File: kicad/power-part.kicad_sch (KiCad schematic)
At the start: 52 parts, among them Q10 BSS84, Q11 BSS123N, Q12 ZXMP10A17GTA, Q2 IPT015N10N5, Q3 IPT015N10N5, Q4 IPT015N10N5, Q5 IPT015N10N5, Q6 IPT015N10N5, Q7 IPT015N10N5, Q8 IPT015N10N5, Q9 IPT015N10N5

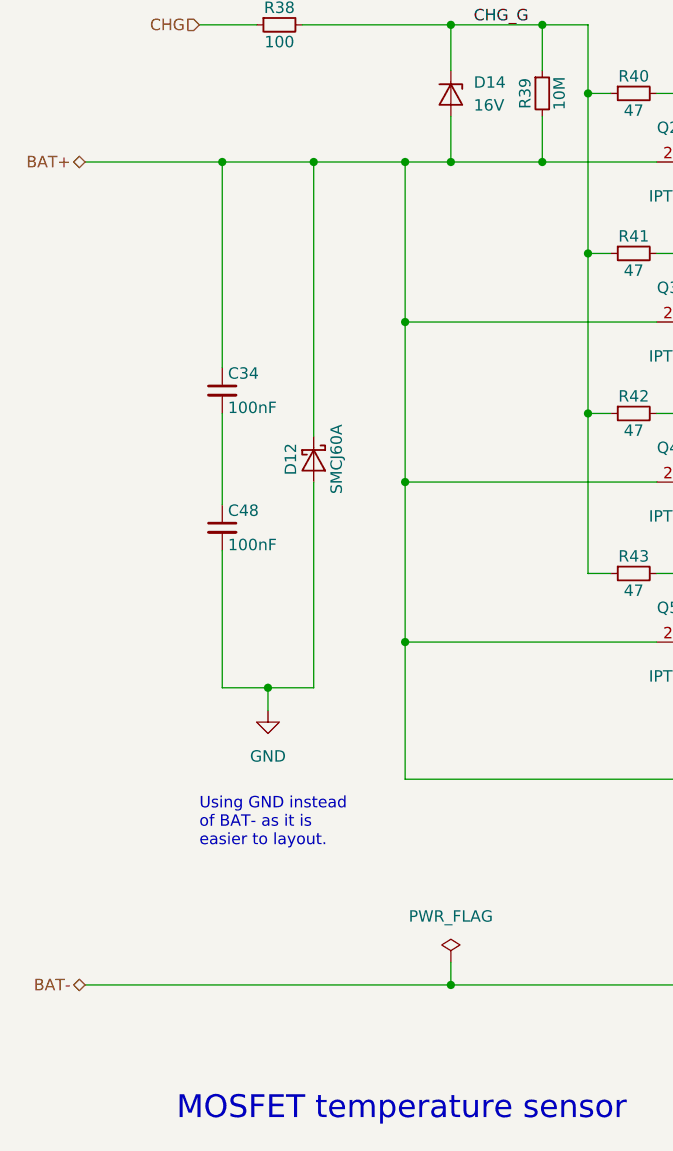
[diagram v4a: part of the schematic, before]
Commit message: v0.3.3: Final version for BMS challenge with EnAccess
Updates compared to v0.3.2:

- Optimization of some copper planes
- Net tie with thicker connection to GND
- D12 connected to Bat-

No parts were changed, the BOM is same as before.
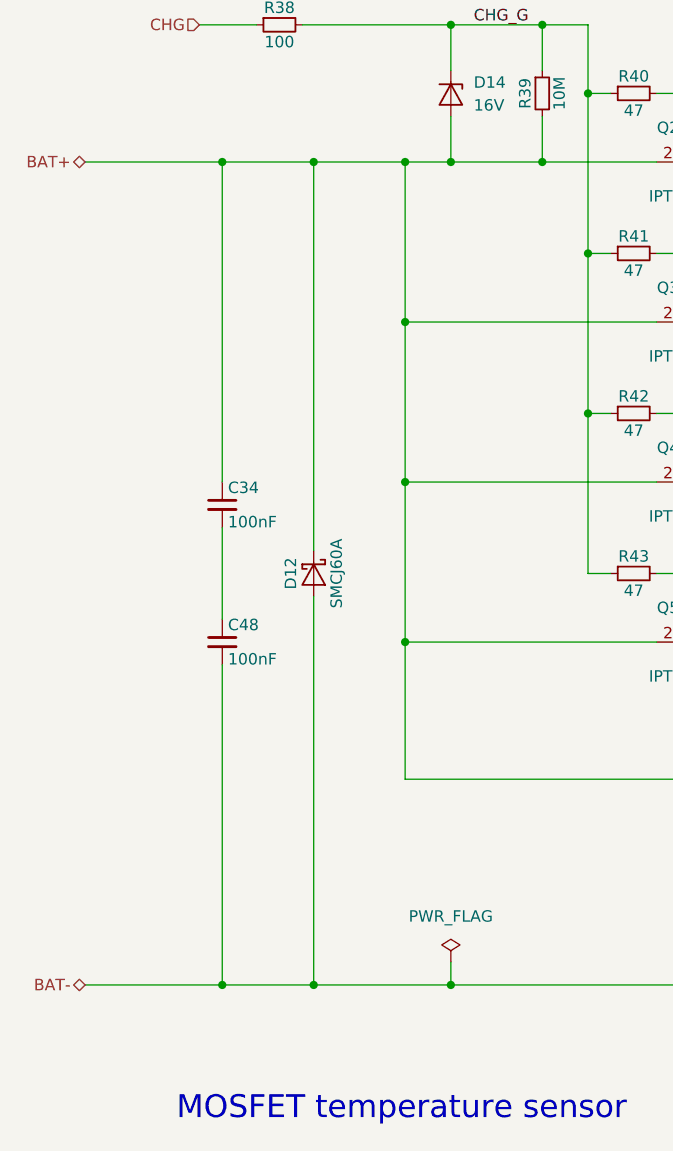
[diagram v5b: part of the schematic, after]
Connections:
- net BAT-: now also C48.2, D12.2 (A)
- net GND: no longer C48.2, D12.2 (A)
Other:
- note removed: "Using GND instead of BAT- as it is easier to layout."
- moved on the sheet: C34, C48, D12
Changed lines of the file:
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@@
   (title_block
     (title "Libre Solar BMS C1")
-    (date "2022-11-07")
-    (rev "0.3.2")
+    (date "2022-11-21")
+    (rev "0.3.3")
     (company "Libre Solar Technologies GmbH")
     (comment 1 "Website: https://libre.solar")
@@
   (junction (at 187.96 43.18) (diameter 0) (color 0 0 0 0)
   )
-  (junction (at 48.26 127) (diameter 0) (color 0 0 0 0)
-  )
   (junction (at 114.3 86.36) (diameter 0) (color 0 0 0 0)
   )
@@
   (junction (at 254 68.58) (diameter 0) (color 0 0 0 0)
   )
+  (junction (at 53.34 160.02) (diameter 0) (color 0 0 0 0)
+  )
   (junction (at 83.82 78.74) (diameter 0) (color 0 0 0 0)
   )
@@
   (junction (at 106.68 68.58) (diameter 0) (color 0 0 0 0)
   )
+  (junction (at 43.18 160.02) (diameter 0) (color 0 0 0 0)
+  )
   (junction (at 134.62 27.94) (diameter 0) (color 0 0 0 0)
   )
@@
     (stroke (width 0) (type default) (color 0 0 0 0))
   )
-  (wire (pts (xy 43.18 111.76) (xy 43.18 127))
+  (wire (pts (xy 43.18 124.46) (xy 43.18 160.02))
     (stroke (width 0) (type default) (color 0 0 0 0))
   )
@@
     (stroke (width 0) (type default) (color 0 0 0 0))
   )
-  (wire (pts (xy 53.34 68.58) (xy 53.34 99.06))
+  (wire (pts (xy 53.34 68.58) (xy 53.34 111.76))
     (stroke (width 0) (type default) (color 0 0 0 0))
   )
@@
     (stroke (width 0) (type default) (color 0 0 0 0))
   )
-  (wire (pts (xy 48.26 127) (xy 48.26 129.54))
-    (stroke (width 0) (type default) (color 0 0 0 0))
-  )
   (wire (pts (xy 172.72 53.34) (xy 177.8 53.34))
     (stroke (width 0) (type default) (color 0 0 0 0))
@@
     (stroke (width 0) (type default) (color 0 0 0 0))
   )
-  (wire (pts (xy 53.34 104.14) (xy 53.34 127))
+  (wire (pts (xy 53.34 116.84) (xy 53.34 160.02))
     (stroke (width 0) (type default) (color 0 0 0 0))
   )
@@
     (stroke (width 0) (type default) (color 0 0 0 0))
   )
+  (wire (pts (xy 53.34 160.02) (xy 68.58 160.02))
+    (stroke (width 0) (type default) (color 0 0 0 0))
+  )
   (wire (pts (xy 177.8 53.34) (xy 180.34 53.34))
     (stroke (width 0) (type default) (color 0 0 0 0))
@@
     (stroke (width 0) (type solid) (color 0 0 0 0))
   )
-  (wire (pts (xy 48.26 127) (xy 43.18 127))
-    (stroke (width 0) (type default) (color 0 0 0 0))
-  )
-  (wire (pts (xy 53.34 127) (xy 48.26 127))
-    (stroke (width 0) (type default) (color 0 0 0 0))
-  )
   (wire (pts (xy 139.7 114.3) (xy 142.24 114.3))
     (stroke (width 0) (type default) (color 0 0 0 0))
@@
     (stroke (width 0) (type default) (color 0 0 0 0))
   )
-  (wire (pts (xy 27.94 160.02) (xy 68.58 160.02))
+  (wire (pts (xy 27.94 160.02) (xy 43.18 160.02))
     (stroke (width 0) (type default) (color 0 0 0 0))
   )
@@
     (stroke (width 0) (type default) (color 0 0 0 0))
   )
+  (wire (pts (xy 43.18 160.02) (xy 53.34 160.02))
+    (stroke (width 0) (type default) (color 0 0 0 0))
+  )
   (wire (pts (xy 68.58 157.48) (xy 68.58 160.02))
     (stroke (width 0) (type default) (color 0 0 0 0))
@@
     (stroke (width 0) (type solid) (color 0 0 0 0))
   )
-  (wire (pts (xy 43.18 68.58) (xy 43.18 91.44))
+  (wire (pts (xy 43.18 68.58) (xy 43.18 104.14))
     (stroke (width 0) (type default) (color 0 0 0 0))
   )
@@
     (stroke (width 0) (type solid) (color 0 0 0 0))
   )
-  (wire (pts (xy 43.18 96.52) (xy 43.18 106.68))
+  (wire (pts (xy 43.18 109.22) (xy 43.18 119.38))
     (stroke (width 0) (type solid) (color 0 0 0 0))
   )
@@
     (effects (font (size 2.54 2.54)) (justify left bottom))
   )
-  (text "Using GND instead\nof BAT- as it is\neasier to layout."
-    (at 40.64 144.78 0)
-    (effects (font (size 1.27 1.27)) (justify left bottom))
-  )
   (text "Bus precharge circuit" (at 187.96 86.36 0)
     (effects (font (size 2.54 2.54)) (justify left bottom))
@@
     (pin "2")
   )
-  (symbol (lib_id "LibreSolar:D_Schottky") (at 53.34 101.6 90) (mirror x) (unit 1)
-    (in_bom yes) (on_board yes)
-    (property "Reference" "D12" (id 0) (at 50.8 101.6 0))
-    (property "Value" "SMCJ60A" (id 1) (at 55.88 101.6 0))
-    (property "Footprint" "LibreSolar:D_SMC" (id 2) (at 53.34 101.6 90)
-      (effects (font (size 1.27 1.27)) hide)
-    )
-    (property "Datasheet" "" (id 3) (at 53.34 101.6 90))
-    (property "Manufacturer" "Bourns" (id 4) (at 53.34 101.6 0)
-      (effects (font (size 1.524 1.524)) hide)
-    )
-    (property "PartNumber" "SMCJ60A" (id 5) (at 53.34 101.6 0)
-      (effects (font (size 1.524 1.524)) hide)
-    )
-    (property "Remarks" "Alternative: Diodes Inc. SMCJ60A-13-F" (id 7) (at 53.34 101.6 0)
+  (symbol (lib_id "LibreSolar:D_Schottky") (at 53.34 114.3 90) (mirror x) (unit 1)
+    (in_bom yes) (on_board yes)
+    (property "Reference" "D12" (id 0) (at 50.8 114.3 0))
+    (property "Value" "SMCJ60A" (id 1) (at 55.88 114.3 0))
+    (property "Footprint" "LibreSolar:D_SMC" (id 2) (at 53.34 114.3 90)
+      (effects (font (size 1.27 1.27)) hide)
+    )
+    (property "Datasheet" "" (id 3) (at 53.34 114.3 90))
+    (property "Manufacturer" "Bourns" (id 4) (at 53.34 114.3 0)
+      (effects (font (size 1.524 1.524)) hide)
+    )
+    (property "PartNumber" "SMCJ60A" (id 5) (at 53.34 114.3 0)
+      (effects (font (size 1.524 1.524)) hide)
+    )
+    (property "Remarks" "Alternative: Diodes Inc. SMCJ60A-13-F" (id 7) (at 53.34 114.3 0)
       (effects (font (size 1.27 1.27)) hide)
     )
@@
       (effects (font (size 1.27 1.27)) hide)
     )
-    (property "Reference" "R45" (id 7) (at 121.92 160.02 0)
-      (effects (font (size 1.27 1.27)) hide)
-    )
-    (property "Value" "300µ" (id 8) (at 121.92 160.02 0)
-      (effects (font (size 1.27 1.27)) hide)
-    )
     (pin "1")
     (pin "2")
@@
     (pin "2")
     (pin "3")
-  )
-  (symbol (lib_id "power:GND") (at 48.26 129.54 0) (unit 1)
-    (in_bom yes) (on_board yes) (fields_autoplaced)
-    (property "Reference" "#PWR0150" (id 0) (at 48.26 135.89 0)
-      (effects (font (size 1.27 1.27)) hide)
-    )
-    (property "Value" "GND" (id 1) (at 48.26 134.62 0))
-    (property "Footprint" "" (id 2) (at 48.26 129.54 0)
-      (effects (font (size 1.27 1.27)) hide)
-    )
-    (property "Datasheet" "" (id 3) (at 48.26 129.54 0)
-      (effects (font (size 1.27 1.27)) hide)
-    )
-    (pin "1")
   )
   (symbol (lib_id "LibreSolar:R") (at 200.66 109.22 90) (mirror x) (unit 1)
@@
     (pin "1")
   )
-  (symbol (lib_id "LibreSolar:C") (at 43.18 109.22 0) (unit 1)
-    (in_bom yes) (on_board yes)
-    (property "Reference" "C48" (id 0) (at 43.815 107.315 0)
-      (effects (font (size 1.27 1.27)) (justify left))
-    )
-    (property "Value" "100nF" (id 1) (at 43.815 111.125 0)
-      (effects (font (size 1.27 1.27)) (justify left))
-    )
-    (property "Footprint" "LibreSolar:C_0603_1608" (id 2) (at 43.18 114.3 0)
-      (effects (font (size 1.27 1.27)) hide)
-    )
-    (property "Datasheet" "" (id 3) (at 43.815 107.315 0))
-    (property "Manufacturer" "any" (id 4) (at -109.22 215.9 0)
-      (effects (font (size 1.524 1.524)) hide)
-    )
-    (property "PartNumber" "" (id 5) (at -109.22 215.9 0)
-      (effects (font (size 1.524 1.524)) hide)
-    )
-    (property "Remarks" "X7R, 100V" (id 6) (at 43.18 109.22 0)
+  (symbol (lib_id "LibreSolar:C") (at 43.18 121.92 0) (unit 1)
+    (in_bom yes) (on_board yes)
+    (property "Reference" "C48" (id 0) (at 43.815 120.015 0)
+      (effects (font (size 1.27 1.27)) (justify left))
+    )
+    (property "Value" "100nF" (id 1) (at 43.815 123.825 0)
+      (effects (font (size 1.27 1.27)) (justify left))
+    )
+    (property "Footprint" "LibreSolar:C_0603_1608" (id 2) (at 43.18 127 0)
+      (effects (font (size 1.27 1.27)) hide)
+    )
+    (property "Datasheet" "" (id 3) (at 43.815 120.015 0))
+    (property "Manufacturer" "any" (id 4) (at -109.22 228.6 0)
+      (effects (font (size 1.524 1.524)) hide)
+    )
+    (property "PartNumber" "" (id 5) (at -109.22 228.6 0)
+      (effects (font (size 1.524 1.524)) hide)
+    )
+    (property "Remarks" "X7R, 100V" (id 6) (at 43.18 121.92 0)
       (effects (font (size 1.27 1.27)) hide)
     )
@@
     (pin "2")
   )
-  (symbol (lib_id "LibreSolar:C") (at 43.18 93.98 0) (unit 1)
-    (in_bom yes) (on_board yes)
-    (property "Reference" "C34" (id 0) (at 43.815 92.075 0)
-      (effects (font (size 1.27 1.27)) (justify left))
-    )
-    (property "Value" "100nF" (id 1) (at 43.815 95.885 0)
-      (effects (font (size 1.27 1.27)) (justify left))
-    )
-    (property "Footprint" "LibreSolar:C_0603_1608" (id 2) (at 43.18 99.06 0)
-      (effects (font (size 1.27 1.27)) hide)
-    )
-    (property "Datasheet" "" (id 3) (at 43.815 92.075 0))
-    (property "Manufacturer" "any" (id 4) (at -109.22 190.5 0)
-      (effects (font (size 1.524 1.524)) hide)
-    )
-    (property "PartNumber" "" (id 5) (at -109.22 190.5 0)
-      (effects (font (size 1.524 1.524)) hide)
-    )
-    (property "Remarks" "X7R, 100V" (id 6) (at 43.18 93.98 0)
-      (effects (font (size 1.27 1.27)) hide)
-    )
+  (symbol (lib_id "LibreSolar:C") (at 43.18 106.68 0) (unit 1)
+    (in_bom yes) (on_board yes)
+    (property "Reference" "C34" (id 0) (at 43.815 104.775 0)
+      (effects (font (size 1.27 1.27)) (justify left))
+    )
+    (property "Value" "100nF" (id 1) (at 43.815 108.585 0)
+      (effects (font (size 1.27 1.27)) (justify left))
+    )
+    (property "Footprint" "LibreSolar:C_0603_1608" (id 2) (at 43.18 111.76 0)
+      (effects (font (size 1.27 1.27)) hide)
+    )
+    (property "Datasheet" "" (id 3) (at 43.815 104.775 0))
+    (property "Manufacturer" "any" (id 4) (at -109.22 203.2 0)
+      (effects (font (size 1.524 1.524)) hide)
+    )
+    (property "PartNumber" "" (id 5) (at -109.22 203.2 0)
+      (effects (font (size 1.524 1.524)) hide)
+    )
+    (property "Remarks" "X7R, 100V" (id 6) (at 43.18 106.68 0)
+      (effects (font (size 1.27 1.27)) hide)
+    )
